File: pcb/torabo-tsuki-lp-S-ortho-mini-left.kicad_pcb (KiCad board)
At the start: 2 copper layers, 123.8 x 71.8 mm, 56 parts, among them J101 Conn_01x06_MountingPin, SW10 SW_Push, SW101 SW_SPDT, SW11 SW_Push, SW12 SW_Push, SW13 SW_Push, SW16 SW_Push, SW17 SW_Push, SW18 SW_Push, SW19 SW_Push, SW20 SW_Push, SW23 SW_Push, SW24 SW_Push, SW25 SW_Push, SW26 SW_Push, SW27 SW_Push, SW28 SW_Push, SW30 SW_Push, SW31 SW_Push, SW32 SW_Push, SW33 SW_Push, SW34 SW_Push, SW35 SW_Push, SW9 SW_Push, U101 BLEMicroPro

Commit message: Add outer key columns to split PCBs
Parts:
- added D15: D_Small, Library:D_SOD-123_HandSoldering, B.Cu at (20.5, 64.1)
- added D22: D_Small, Library:D_SOD-123_HandSoldering, B.Cu at (20.5, 81.1)
- added D29: D_Small, Library:D_SOD-123_HandSoldering, B.Cu at (20.5, 98.1)
- added D8: D_Small, Library:D_SOD-123_HandSoldering, B.Cu at (20.5, 47.1)
- added SW15: SW_Push, Library:CHOC_V2_SOCKET_HANDSOLDERING_17mm, B.Cu at (19.0, 68.0)
- added SW22: SW_Push, Library:CHOC_V2_SOCKET_HANDSOLDERING_17mm, B.Cu at (19.0, 85.0)
- added SW29: SW_Push, Library:CHOC_V2_SOCKET_HANDSOLDERING_17mm, B.Cu at (19.0, 102.0)
- added SW8: SW_Push, Library:CHOC_V2_SOCKET_HANDSOLDERING_17mm, B.Cu at (19.0, 51.0)
- moved REF** 17.0 mm to (10.5, 41.5)
- moved REF** 17.0 mm to (10.5, 111.5)
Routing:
- net /left/COL0: track 0.00 -> 194.8 mm, vias 0 -> 2
- net /left/ROW2: track 111.4 -> 130.0 mm, vias 5 -> 6
- net /left/ROW1: track 108.9 -> 127.4 mm, vias 6 -> 7
- net /left/ROW4: track 137.1 -> 155.6 mm, vias 7 -> 8
- net /left/ROW3: track 141.3 -> 159.8 mm, vias 7 -> 8
- net Net-(D29-K): track 0.00 -> 9.80 mm
- net Net-(D22-K): track 0.00 -> 9.80 mm
- net Net-(D15-K): track 0.00 -> 9.80 mm
- net Net-(D8-K): track 0.00 -> 9.80 mm
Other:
- board size 123.8 x 71.8 mm -> 140.8 x 71.8 mm

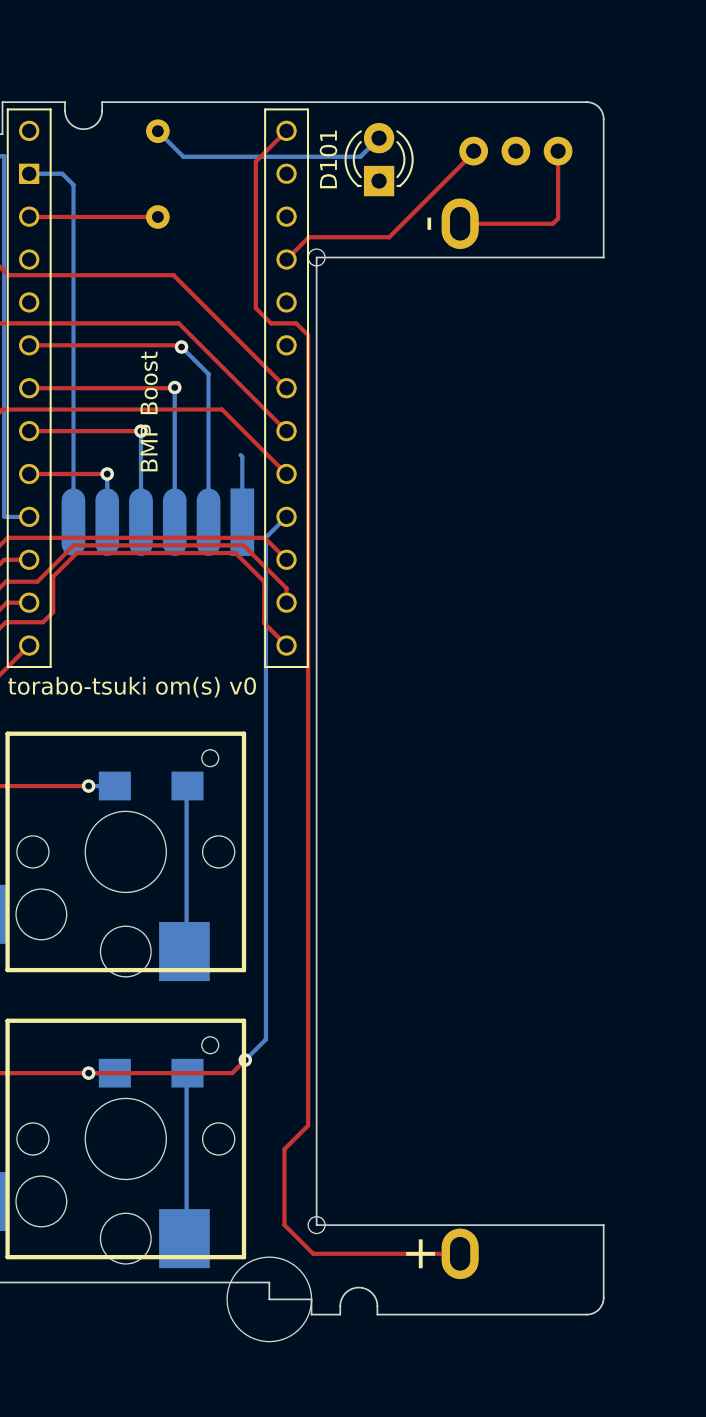
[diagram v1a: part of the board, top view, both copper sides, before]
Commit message: Adapt split keyboard PCBs for AAA battery holders
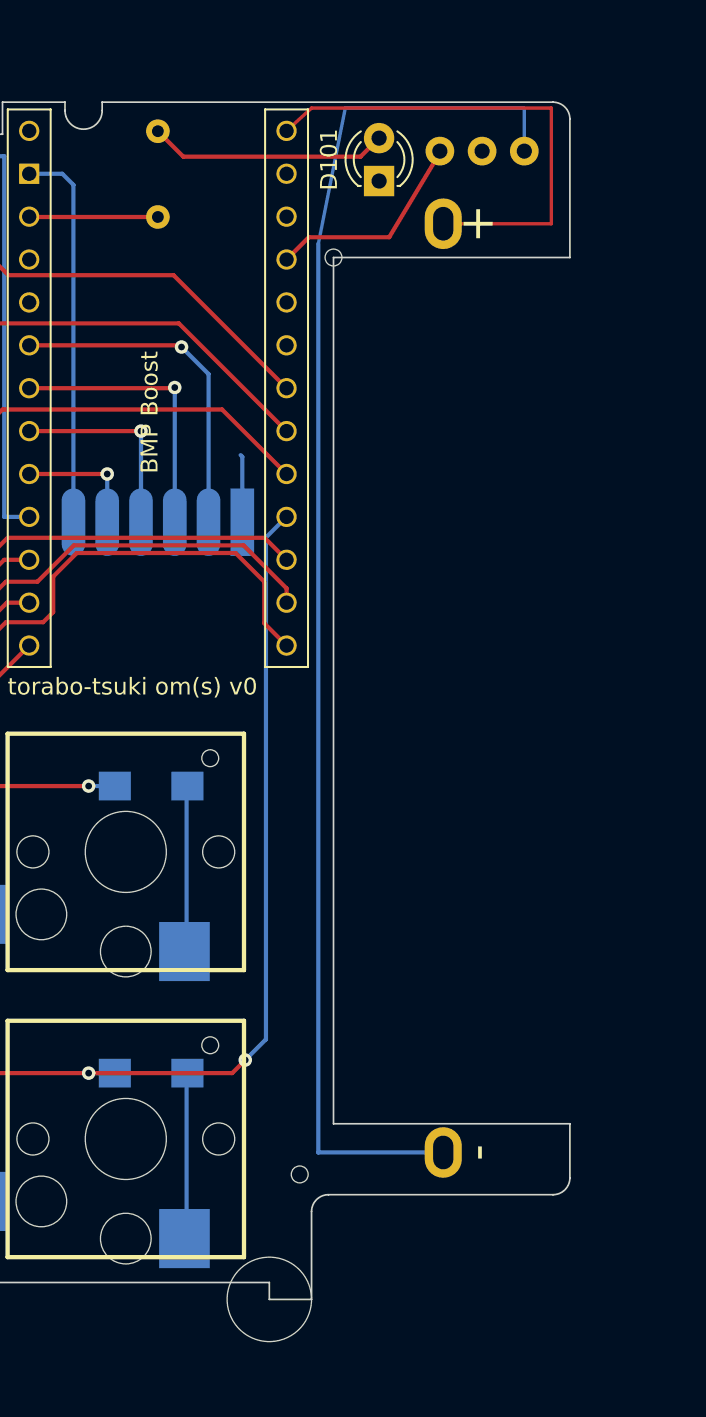
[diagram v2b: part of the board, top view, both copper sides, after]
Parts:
- BT101: footprint Library:battery_holder -> Library:battery_holder_AAA_1x_P55mm
- moved BT101 3.16 mm to (139.8, 75.3), turned to 90 degrees
- moved REF** 3.16 mm to (133.4, 104.1)
- moved SW101 2.00 mm to (142.1, 43.5)
- moved REF** 1.00 mm to (133.3, 49.8)
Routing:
- net Net-(BT101--): track 9.92 -> 82.6 mm
- net +BATT: track 79.4 -> 29.5 mm
- net /left/BOOT: track 13.8 -> 12.6 mm
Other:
- board size 140.8 x 71.8 mm -> 138.8 x 70.9 mm

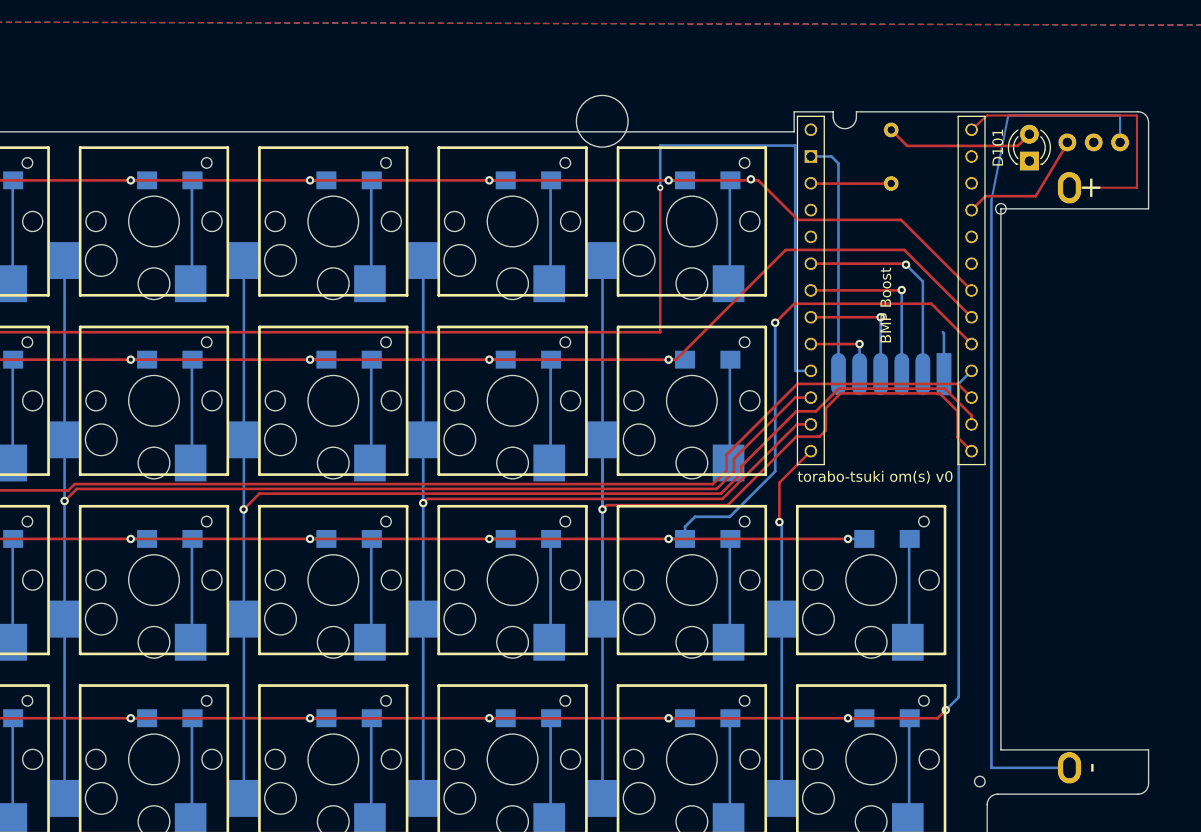
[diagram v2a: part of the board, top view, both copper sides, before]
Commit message: Migrate split PCBs to XIAO nRF52840 Plus
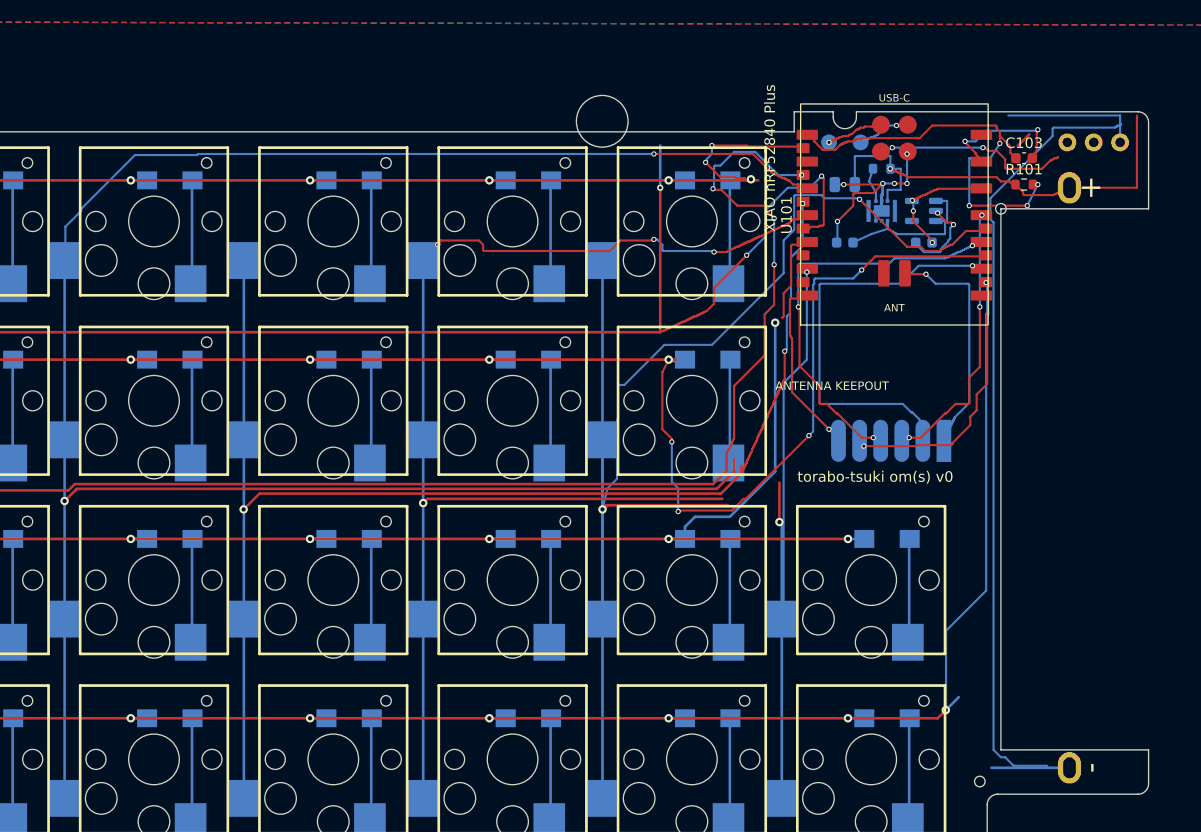
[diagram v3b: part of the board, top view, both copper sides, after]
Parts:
- removed D101: LED_Small, Library:LED_D3.0mm
- added C101: 10uF X7R (CIN), C_0805_2012Metric, B.Cu at (118.5, 47.5)
- added C102: 10uF X7R (CL), C_0603_1608Metric, B.Cu at (118.5, 53.0)
- added C103: 0.1uF X7R, C_0603_1608Metric, F.Cu at (135.5, 45.0)
- added C104: 0.1uF X7R, C_0603_1608Metric, B.Cu at (126.0, 53.0)
- added R102: 100k, R_0603_1608Metric, B.Cu at (122.0, 46.0)
- added TP101: SWDIO, TestPoint_Pad_D1.5mm, B.Cu at (117.0, 43.5)
- added TP102: SWDCLK, TestPoint_Pad_D1.5mm, B.Cu at (120.0, 43.5)
- added U102: XCL103D333CR-G, CL-2025-02, B.Cu at (122.0, 50.0)
- added U103: XC8111AA01MR-G, SOT-23-5, B.Cu at (126.0, 50.0)
- R101: value 330 -> 10k; footprint Library:R_Axial_DIN0204_L3.6mm_D1.6mm_P5.08mm_Horizontal -> R_0603_1608Metric; moved to F.Cu
- U101: value BLEMicroPro -> XIAO nRF52840 Plus; footprint Library:BLEMicroPro -> XIAO-nRF52840-Plus-SMD
- moved R101 12.6 mm to (135.5, 47.5), turned to 0 degrees
- moved U101 8.11 mm to (123.2, 50.4), turned to 90 degrees
- moved J101 6.33 mm to (122.9, 71.8)
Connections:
- R101 pad 1: /left/LED -> +BATT
- R101 pad 2: Net-(D101-A) -> /left/VBAT_ADC
- SW101 pad 1: /left/BOOT -> /left/RESET_N
- U101 pad 1: GND -> /left/VBAT_ADC
- U101 pad 10: /left/COL0 -> /left/MOTION
- U101 pad 11: /left/COL2 -> /left/SDIO
- U101 pad 12: /left/COL4 -> /left/SYS_3V3
- U101 pad 13: /left/COL6 -> GND
- U101 pad 14: /left/COL5 -> (no net)
- U101 pad 15: /left/COL3 -> /left/ROW1
- U101 pad 17: /left/ROW4 -> /left/COL3
- U101 pad 18: /left/ROW3 -> /left/COL0
- U101 pad 19: /left/ROW2 -> (no net)
- U101 pad 2: VCC -> /left/ROW0
- U101 pad 20: /left/ROW1 -> (no net)
- U101 pad 21: /left/ROW0 -> /left/ROW4
- U101 pad 22: unconnected-(U101-4V3-Pad22) -> /left/ROW2
- U101 pad 23: /left/BOOT -> /left/COL5
- U101 pad 24: GND -> /left/SWDIO
- U101 pad 25: unconnected-(U101-+5V-Pad25) -> /left/SWDCLK
- U101 pad 26: +BATT -> /left/RESET_N
- U101 pad 3: /left/LED -> /left/COL2
- U101 pad 4: GND -> /left/COL4
- U101 pad 5: unconnected-(U101-GND-Pad5) -> /left/ROW3
- U101 pad 6: /left/SCLK -> /left/COL6
- U101 pad 7: /left/SDIO -> VCC
- U101 pad 8: /left/MOTION -> /left/CS
- U101 pad 9: /left/CS -> /left/SCLK
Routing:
- net /left/COL2: track 126.5 -> 194.8 mm, vias 1 -> 2
- net GND: track 4.02 -> 72.2 mm, vias 0 -> 11
- net /left/VBAT_ADC: track 0.00 -> 40.5 mm, vias 0 -> 4
- net /left/COL6: track 34.2 -> 64.3 mm, vias 1 -> 2
- net /left/COL5: track 112.5 -> 142.1 mm, vias 1 -> 2
- net /left/ROW2: track 130.0 -> 159.6 mm, vias 6 -> 11
- net /left/COL4: track 90.8 -> 120.3 mm, vias 1 -> 4
- net /left/MOTION: track 12.0 -> 39.6 mm, vias 1 -> 3
- net /left/SCLK: track 20.1 -> 39.8 mm
- net /left/RESET_N: track 0.00 -> 18.9 mm, vias 0 -> 2
- net /left/CS: track 7.48 -> 25.1 mm
- net /left/COL1: track 159.6 -> 176.5 mm, vias 1 -> 5
- net /left/BOOST_3V3: track 0.00 -> 16.8 mm
- net +BATT: track 29.5 -> 44.3 mm, vias 0 -> 1
- net Net-(D101-A): track 14.2 -> 1.56 mm
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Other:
- board text added: "ANTENNA KEEPOUT"
- board text added: "XIAO nRF52840 Plus"
- board text removed: "BMP Boost"

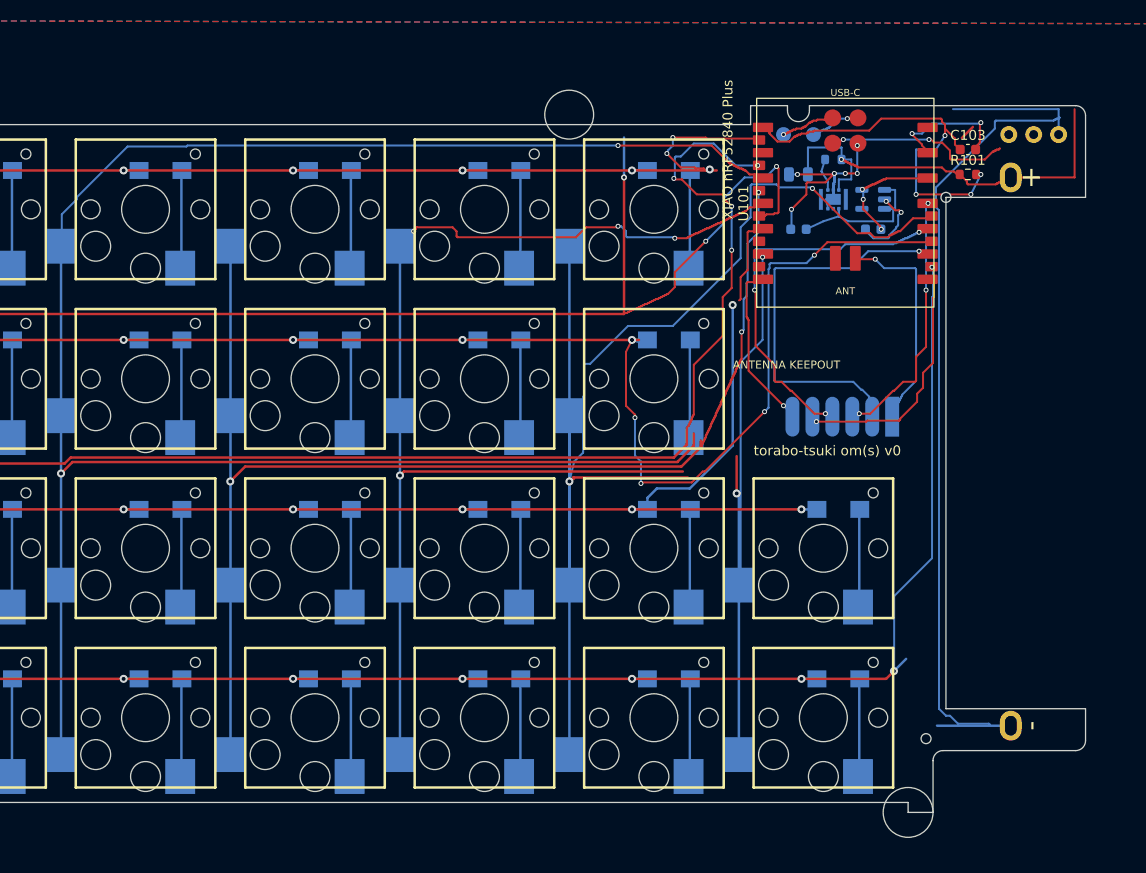
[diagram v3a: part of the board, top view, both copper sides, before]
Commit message: Compact XIAO and battery PCB layout
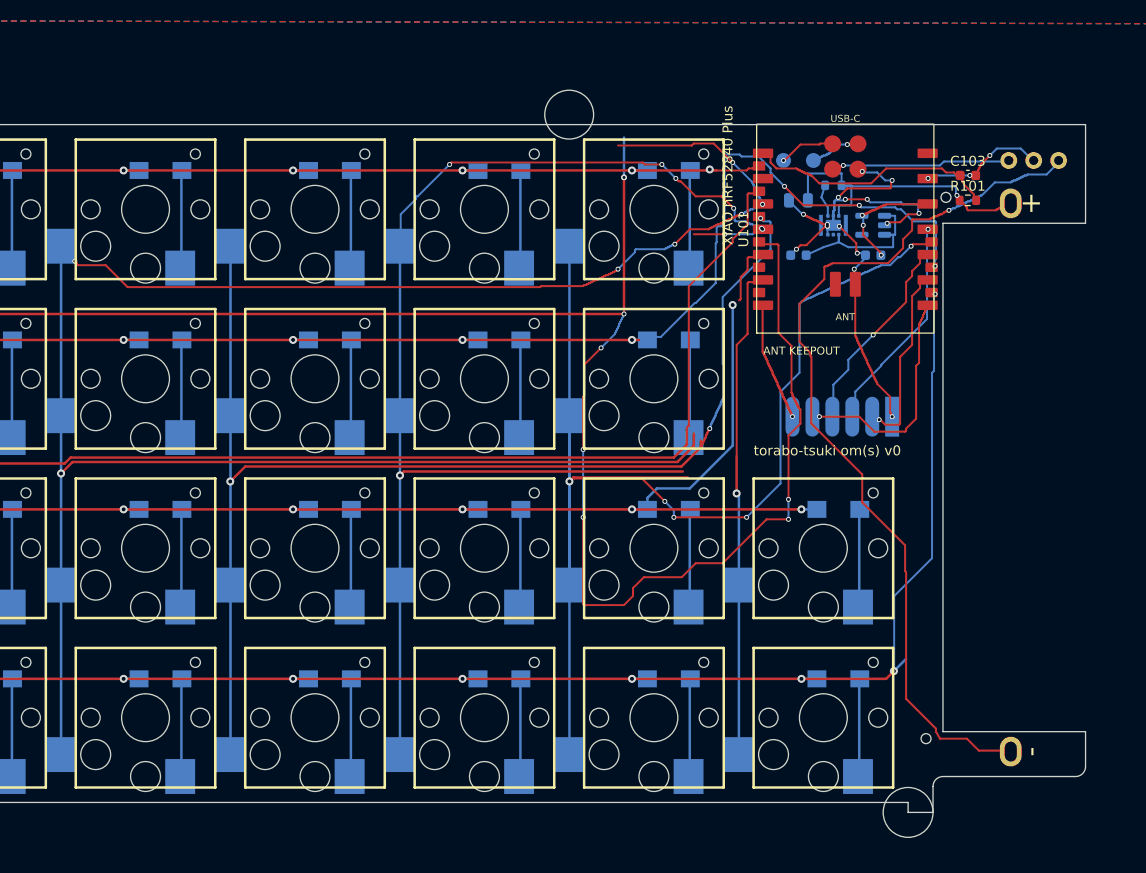
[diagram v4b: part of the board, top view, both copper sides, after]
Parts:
- moved C101 2.60 mm to (118.5, 50.1)
- moved C102 2.60 mm to (118.5, 55.6)
- moved C103 2.60 mm to (135.5, 47.6)
- moved C104 2.60 mm to (126.0, 55.6)
- moved R101 2.60 mm to (135.5, 50.1)
- moved R102 2.60 mm to (122.0, 48.6)
- moved SW101 2.60 mm to (142.1, 46.1)
- moved TP101 2.60 mm to (117.0, 46.1)
- moved TP102 2.60 mm to (120.0, 46.1)
- moved U101 2.60 mm to (123.2, 53.0)
- moved U102 2.60 mm to (122.0, 52.6)
- moved U103 2.60 mm to (126.0, 52.6)
- moved BT101 2.60 mm to (139.8, 77.9)
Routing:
- net /left/COL0: track 189.9 -> 245.7 mm, vias 4 -> 8
- net /left/SCLK: track 39.8 -> 19.1 mm
- net /left/MOTION: track 39.6 -> 20.6 mm, vias 3 -> 1
- net /left/COL1: track 176.5 -> 160.5 mm, vias 5 -> 1
- net /left/COL2: track 194.8 -> 210.6 mm, vias 2 -> 7
- net /left/VBAT_ADC: track 40.5 -> 25.6 mm, vias 4 -> 0
- net /left/COL6: track 64.3 -> 49.5 mm, vias 2 -> 1
- net /left/ROW2: track 159.6 -> 146.8 mm, vias 11 -> 9
- net +BATT: track 44.3 -> 31.6 mm
- net /left/COL4: track 120.3 -> 132.0 mm, vias 4 -> 8
- net /left/ROW1: track 118.6 -> 108.0 mm, vias 9 -> 7
- net GND: track 72.2 -> 76.9 mm, vias 11 -> 18
- net VCC: track 17.1 -> 12.5 mm
- net /left/SDIO: track 26.2 -> 22.0 mm, vias 3 -> 1
- net Net-(BT101--): track 94.5 -> 90.9 mm, vias 0 -> 1
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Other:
- board size 138.8 x 70.9 mm -> 138.8 x 69 mm
- board text added: "ANT KEEPOUT"
- board text removed: "ANTENNA KEEPOUT"
